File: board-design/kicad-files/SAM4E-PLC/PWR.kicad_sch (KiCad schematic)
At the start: 18 parts, among them Q1 BC817, U14 LM2576HVS-3.3

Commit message: [UPDATE]
Work in progress.

Signed-off-by: Nicolae-Andrei Vasile <vasilenicolaeandrei@gmail.com>
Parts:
- renumbered D35 to D36
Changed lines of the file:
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@@
         )
         (path "/93076d8a-73da-4f5d-b7f2-28678f1db77d/aee81a7b-cba1-4b89-a883-459d3f783e91"
-          (reference "C93") (unit 1)
+          (reference "C95") (unit 1)
         )
       )
@@
         )
         (path "/93076d8a-73da-4f5d-b7f2-28678f1db77d/aee81a7b-cba1-4b89-a883-459d3f783e91"
-          (reference "C90") (unit 1)
+          (reference "C92") (unit 1)
         )
       )
@@
         )
         (path "/93076d8a-73da-4f5d-b7f2-28678f1db77d/aee81a7b-cba1-4b89-a883-459d3f783e91"
-          (reference "C95") (unit 1)
+          (reference "C97") (unit 1)
         )
       )
@@
   (symbol (lib_id "power:GND") (at 234.95 133.35 0) (unit 1)
     (in_bom yes) (on_board yes) (dnp no) (fields_autoplaced)
-    (property "Reference" "#PWR085" (at 234.95 139.7 0)
+    (property "Reference" "#PWR086" (at 234.95 139.7 0)
       (effects (font (size 1.27 1.27)) hide)
     )
@@
       (project "SAM4E-PLC"
         (path "/93076d8a-73da-4f5d-b7f2-28678f1db77d/aee81a7b-cba1-4b89-a883-459d3f783e91"
-          (reference "#PWR085") (unit 1)
+          (reference "#PWR086") (unit 1)
         )
       )
@@
   (symbol (lib_id "power:+3V3") (at 245.11 93.98 0) (unit 1)
     (in_bom yes) (on_board yes) (dnp no) (fields_autoplaced)
-    (property "Reference" "#PWR086" (at 245.11 97.79 0)
+    (property "Reference" "#PWR087" (at 245.11 97.79 0)
       (effects (font (size 1.27 1.27)) hide)
     )
@@
       (project "SAM4E-PLC"
         (path "/93076d8a-73da-4f5d-b7f2-28678f1db77d/aee81a7b-cba1-4b89-a883-459d3f783e91"
-          (reference "#PWR086") (unit 1)
+          (reference "#PWR087") (unit 1)
         )
       )
@@
         )
         (path "/93076d8a-73da-4f5d-b7f2-28678f1db77d/aee81a7b-cba1-4b89-a883-459d3f783e91"
-          (reference "C91") (unit 1)
+          (reference "C93") (unit 1)
         )
       )
@@
         )
         (path "/93076d8a-73da-4f5d-b7f2-28678f1db77d/aee81a7b-cba1-4b89-a883-459d3f783e91"
-          (reference "D36") (unit 1)
+          (reference "D37") (unit 1)
         )
       )
@@
   (symbol (lib_id "power:+24V") (at 76.2 88.9 0) (unit 1)
     (in_bom yes) (on_board yes) (dnp no) (fields_autoplaced)
-    (property "Reference" "#PWR083" (at 76.2 92.71 0)
+    (property "Reference" "#PWR084" (at 76.2 92.71 0)
       (effects (font (size 1.27 1.27)) hide)
     )
@@
       (project "SAM4E-PLC"
         (path "/93076d8a-73da-4f5d-b7f2-28678f1db77d/aee81a7b-cba1-4b89-a883-459d3f783e91"
-          (reference "#PWR083") (unit 1)
+          (reference "#PWR084") (unit 1)
         )
       )
@@
   (symbol (lib_id "power:GND") (at 127 113.03 0) (unit 1)
     (in_bom yes) (on_board yes) (dnp no) (fields_autoplaced)
-    (property "Reference" "#PWR084" (at 127 119.38 0)
+    (property "Reference" "#PWR085" (at 127 119.38 0)
       (effects (font (size 1.27 1.27)) hide)
     )
@@
       (project "SAM4E-PLC"
         (path "/93076d8a-73da-4f5d-b7f2-28678f1db77d/aee81a7b-cba1-4b89-a883-459d3f783e91"
-          (reference "#PWR084") (unit 1)
+          (reference "#PWR085") (unit 1)
         )
       )
@@
         )
         (path "/93076d8a-73da-4f5d-b7f2-28678f1db77d/aee81a7b-cba1-4b89-a883-459d3f783e91"
-          (reference "C89") (unit 1)
+          (reference "C91") (unit 1)
         )
       )
@@
         )
         (path "/93076d8a-73da-4f5d-b7f2-28678f1db77d/aee81a7b-cba1-4b89-a883-459d3f783e91"
+          (reference "C96") (unit 1)
+        )
+      )
+    )
+  )
+  (symbol (lib_id "Device:L") (at 152.4 97.79 90) (unit 1)
+    (in_bom yes) (on_board yes) (dnp no)
+    (property "Reference" "L13" (at 152.4 95.25 90)
+      (effects (font (size 1.27 1.27)))
+    )
+    (property "Value" "150uH/12x12mm (SRR1210-151M)" (at 146.05 101.6 90)
+      (effects (font (size 1.27 1.27)))
+    )
+    (property "Footprint" "Inductor_SMD:L_12x12mm_H8mm" (at 152.4 97.79 0)
+      (effects (font (size 1.27 1.27)) hide)
+    )
+    (property "Datasheet" "https://ro.mouser.com/datasheet/2/54/srr1210-1391529.pdf" (at 152.4 97.79 0)
+      (effects (font (size 1.27 1.27)) hide)
+    )
+    (pin "1")
+    (pin "2")
+    (instances
+      (project "SAM4E-PLC"
+        (path "/93076d8a-73da-4f5d-b7f2-28678f1db77d/aee81a7b-cba1-4b89-a883-459d3f783e91"
+          (reference "L13") (unit 1)
+        )
+      )
+    )
+  )
+  (symbol (lib_id "Device:C_Polarized") (at 171.45 104.14 0) (unit 1)
+    (in_bom yes) (on_board yes) (dnp no)
+    (property "Reference" "C5" (at 172.72 109.22 90)
+      (effects (font (size 1.27 1.27)) (justify left))
+    )
+    (property "Value" "100uF/16V/20%/6.3x7.7mm" (at 172.72 101.6 90)
+      (effects (font (size 1.27 1.27)) (justify left))
+    )
+    (property "Footprint" "Capacitor_SMD:CP_Elec_6.3x7.7" (at 172.4152 107.95 0)
+      (effects (font (size 1.27 1.27)) hide)
+    )
+    (property "Datasheet" "~" (at 171.45 104.14 0)
+      (effects (font (size 1.27 1.27)) hide)
+    )
+    (pin "1")
+    (pin "2")
+    (instances
+      (project "SAM4E-PLC"
+        (path "/93076d8a-73da-4f5d-b7f2-28678f1db77d/32910dfe-b730-4651-8391-975b8cdac59d"
+          (reference "C5") (unit 1)
+        )
+        (path "/93076d8a-73da-4f5d-b7f2-28678f1db77d/62dc9d33-a289-4ad9-a327-b6290b31f4f3"
+          (reference "C12") (unit 1)
+        )
+        (path "/93076d8a-73da-4f5d-b7f2-28678f1db77d/aee81a7b-cba1-4b89-a883-459d3f783e91"
           (reference "C94") (unit 1)
         )
@@
     )
   )
-  (symbol (lib_id "Device:L") (at 152.4 97.79 90) (unit 1)
-    (in_bom yes) (on_board yes) (dnp no)
-    (property "Reference" "L13" (at 152.4 95.25 90)
-      (effects (font (size 1.27 1.27)))
-    )
-    (property "Value" "150uH/12x12mm (SRR1210-151M)" (at 146.05 101.6 90)
-      (effects (font (size 1.27 1.27)))
-    )
-    (property "Footprint" "Inductor_SMD:L_12x12mm_H8mm" (at 152.4 97.79 0)
-      (effects (font (size 1.27 1.27)) hide)
-    )
-    (property "Datasheet" "https://ro.mouser.com/datasheet/2/54/srr1210-1391529.pdf" (at 152.4 97.79 0)
-      (effects (font (size 1.27 1.27)) hide)
-    )
-    (pin "1")
-    (pin "2")
-    (instances
-      (project "SAM4E-PLC"
-        (path "/93076d8a-73da-4f5d-b7f2-28678f1db77d/aee81a7b-cba1-4b89-a883-459d3f783e91"
-          (reference "L13") (unit 1)
-        )
-      )
-    )
-  )
-  (symbol (lib_id "Device:C_Polarized") (at 171.45 104.14 0) (unit 1)
-    (in_bom yes) (on_board yes) (dnp no)
-    (property "Reference" "C5" (at 172.72 109.22 90)
-      (effects (font (size 1.27 1.27)) (justify left))
-    )
-    (property "Value" "100uF/16V/20%/6.3x7.7mm" (at 172.72 101.6 90)
-      (effects (font (size 1.27 1.27)) (justify left))
-    )
-    (property "Footprint" "Capacitor_SMD:CP_Elec_6.3x7.7" (at 172.4152 107.95 0)
-      (effects (font (size 1.27 1.27)) hide)
-    )
-    (property "Datasheet" "~" (at 171.45 104.14 0)
-      (effects (font (size 1.27 1.27)) hide)
-    )
-    (pin "1")
-    (pin "2")
-    (instances
-      (project "SAM4E-PLC"
-        (path "/93076d8a-73da-4f5d-b7f2-28678f1db77d/32910dfe-b730-4651-8391-975b8cdac59d"
-          (reference "C5") (unit 1)
-        )
-        (path "/93076d8a-73da-4f5d-b7f2-28678f1db77d/62dc9d33-a289-4ad9-a327-b6290b31f4f3"
-          (reference "C12") (unit 1)
-        )
-        (path "/93076d8a-73da-4f5d-b7f2-28678f1db77d/aee81a7b-cba1-4b89-a883-459d3f783e91"
-          (reference "C92") (unit 1)
-        )
-      )
-    )
-  )
   (symbol (lib_id "Device:LED") (at 234.95 114.3 90) (unit 1)
     (in_bom yes) (on_board yes) (dnp no)
@@
         )
         (path "/93076d8a-73da-4f5d-b7f2-28678f1db77d/aee81a7b-cba1-4b89-a883-459d3f783e91"
-          (reference "D37") (unit 1)
+          (reference "D38") (unit 1)
         )
       )
@@
   (symbol (lib_id "Device:D_Schottky") (at 63.5 92.71 180) (unit 1)
     (in_bom yes) (on_board yes) (dnp no)
-    (property "Reference" "D35" (at 63.5 87.63 0)
+    (property "Reference" "D36" (at 63.5 87.63 0)
       (effects (font (size 1.27 1.27)))
     )
@@
       (project "SAM4E-PLC"
         (path "/93076d8a-73da-4f5d-b7f2-28678f1db77d/aee81a7b-cba1-4b89-a883-459d3f783e91"
-          (reference "D35") (unit 1)
-        )
-      )
+          (reference "D36") (unit 1)
+        )
+      )

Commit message: [UPDATE]
Work in progress.

Signed-off-by: Nicolae-Andrei Vasile <vasilenicolaeandrei@gmail.com>
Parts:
- renumbered D36 to D34, L13 to L10, U14 to U11
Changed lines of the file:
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@@
           (reference "C5") (unit 1)
         )
-        (path "/93076d8a-73da-4f5d-b7f2-28678f1db77d/62dc9d33-a289-4ad9-a327-b6290b31f4f3"
-          (reference "C12") (unit 1)
-        )
-        (path "/93076d8a-73da-4f5d-b7f2-28678f1db77d/aee81a7b-cba1-4b89-a883-459d3f783e91"
-          (reference "C95") (unit 1)
+        (path "/93076d8a-73da-4f5d-b7f2-28678f1db77d/aee81a7b-cba1-4b89-a883-459d3f783e91"
+          (reference "C71") (unit 1)
         )
       )
@@
           (reference "C5") (unit 1)
         )
-        (path "/93076d8a-73da-4f5d-b7f2-28678f1db77d/62dc9d33-a289-4ad9-a327-b6290b31f4f3"
-          (reference "C12") (unit 1)
-        )
-        (path "/93076d8a-73da-4f5d-b7f2-28678f1db77d/aee81a7b-cba1-4b89-a883-459d3f783e91"
-          (reference "C92") (unit 1)
+        (path "/93076d8a-73da-4f5d-b7f2-28678f1db77d/aee81a7b-cba1-4b89-a883-459d3f783e91"
+          (reference "C68") (unit 1)
         )
       )
@@
         )
         (path "/93076d8a-73da-4f5d-b7f2-28678f1db77d/aee81a7b-cba1-4b89-a883-459d3f783e91"
-          (reference "C97") (unit 1)
+          (reference "C73") (unit 1)
         )
       )
@@
   (symbol (lib_id "power:GND") (at 234.95 133.35 0) (unit 1)
     (in_bom yes) (on_board yes) (dnp no) (fields_autoplaced)
-    (property "Reference" "#PWR086" (at 234.95 139.7 0)
+    (property "Reference" "#PWR070" (at 234.95 139.7 0)
       (effects (font (size 1.27 1.27)) hide)
     )
@@
       (project "SAM4E-PLC"
         (path "/93076d8a-73da-4f5d-b7f2-28678f1db77d/aee81a7b-cba1-4b89-a883-459d3f783e91"
-          (reference "#PWR086") (unit 1)
+          (reference "#PWR070") (unit 1)
         )
       )
@@
   (symbol (lib_id "power:+3V3") (at 245.11 93.98 0) (unit 1)
     (in_bom yes) (on_board yes) (dnp no) (fields_autoplaced)
-    (property "Reference" "#PWR087" (at 245.11 97.79 0)
+    (property "Reference" "#PWR071" (at 245.11 97.79 0)
       (effects (font (size 1.27 1.27)) hide)
     )
@@
       (project "SAM4E-PLC"
         (path "/93076d8a-73da-4f5d-b7f2-28678f1db77d/aee81a7b-cba1-4b89-a883-459d3f783e91"
-          (reference "#PWR087") (unit 1)
+          (reference "#PWR071") (unit 1)
         )
       )
@@
           (reference "C5") (unit 1)
         )
-        (path "/93076d8a-73da-4f5d-b7f2-28678f1db77d/62dc9d33-a289-4ad9-a327-b6290b31f4f3"
-          (reference "C12") (unit 1)
-        )
-        (path "/93076d8a-73da-4f5d-b7f2-28678f1db77d/aee81a7b-cba1-4b89-a883-459d3f783e91"
-          (reference "C93") (unit 1)
+        (path "/93076d8a-73da-4f5d-b7f2-28678f1db77d/aee81a7b-cba1-4b89-a883-459d3f783e91"
+          (reference "C69") (unit 1)
         )
       )
@@
     (instances
       (project "SAM4E-PLC"
-        (path "/93076d8a-73da-4f5d-b7f2-28678f1db77d/62dc9d33-a289-4ad9-a327-b6290b31f4f3"
-          (reference "D3") (unit 1)
-        )
-        (path "/93076d8a-73da-4f5d-b7f2-28678f1db77d/aee81a7b-cba1-4b89-a883-459d3f783e91"
-          (reference "D37") (unit 1)
+        (path "/93076d8a-73da-4f5d-b7f2-28678f1db77d/aee81a7b-cba1-4b89-a883-459d3f783e91"
+          (reference "D35") (unit 1)
         )
       )
@@
   (symbol (lib_id "power:+24V") (at 76.2 88.9 0) (unit 1)
     (in_bom yes) (on_board yes) (dnp no) (fields_autoplaced)
-    (property "Reference" "#PWR084" (at 76.2 92.71 0)
+    (property "Reference" "#PWR068" (at 76.2 92.71 0)
       (effects (font (size 1.27 1.27)) hide)
     )
@@
       (project "SAM4E-PLC"
         (path "/93076d8a-73da-4f5d-b7f2-28678f1db77d/aee81a7b-cba1-4b89-a883-459d3f783e91"
-          (reference "#PWR084") (unit 1)
+          (reference "#PWR068") (unit 1)
         )
       )
@@
   (symbol (lib_id "power:GND") (at 127 113.03 0) (unit 1)
     (in_bom yes) (on_board yes) (dnp no) (fields_autoplaced)
-    (property "Reference" "#PWR085" (at 127 119.38 0)
+    (property "Reference" "#PWR069" (at 127 119.38 0)
       (effects (font (size 1.27 1.27)) hide)
     )
@@
       (project "SAM4E-PLC"
         (path "/93076d8a-73da-4f5d-b7f2-28678f1db77d/aee81a7b-cba1-4b89-a883-459d3f783e91"
-          (reference "#PWR085") (unit 1)
+          (reference "#PWR069") (unit 1)
         )
       )
@@
   (symbol (lib_id "Regulator_Switching:LM2576HVS-3.3") (at 127 95.25 0) (unit 1)
     (in_bom yes) (on_board yes) (dnp no) (fields_autoplaced)
-    (property "Reference" "U14" (at 127 85.09 0)
+    (property "Reference" "U11" (at 127 85.09 0)
       (effects (font (size 1.27 1.27)))
     )
@@
       (project "SAM4E-PLC"
         (path "/93076d8a-73da-4f5d-b7f2-28678f1db77d/aee81a7b-cba1-4b89-a883-459d3f783e91"
-          (reference "U14") (unit 1)
+          (reference "U11") (unit 1)
         )
       )
@@
     (instances
       (project "SAM4E-PLC"
-        (path "/93076d8a-73da-4f5d-b7f2-28678f1db77d/62dc9d33-a289-4ad9-a327-b6290b31f4f3"
-          (reference "Q1") (unit 1)
-        )
-        (path "/93076d8a-73da-4f5d-b7f2-28678f1db77d/aee81a7b-cba1-4b89-a883-459d3f783e91"
-          (reference "Q13") (unit 1)
+        (path "/93076d8a-73da-4f5d-b7f2-28678f1db77d/aee81a7b-cba1-4b89-a883-459d3f783e91"
+          (reference "Q11") (unit 1)
         )
       )
@@
           (reference "C5") (unit 1)
         )
-        (path "/93076d8a-73da-4f5d-b7f2-28678f1db77d/62dc9d33-a289-4ad9-a327-b6290b31f4f3"
-          (reference "C12") (unit 1)
-        )
-        (path "/93076d8a-73da-4f5d-b7f2-28678f1db77d/aee81a7b-cba1-4b89-a883-459d3f783e91"
-          (reference "C91") (unit 1)
+        (path "/93076d8a-73da-4f5d-b7f2-28678f1db77d/aee81a7b-cba1-4b89-a883-459d3f783e91"
+          (reference "C67") (unit 1)
         )
       )
@@
           (reference "R9") (unit 1)
         )
-        (path "/93076d8a-73da-4f5d-b7f2-28678f1db77d/62dc9d33-a289-4ad9-a327-b6290b31f4f3"
-          (reference "R?") (unit 1)
-        )
         (path "/93076d8a-73da-4f5d-b7f2-28678f1db77d/f76e13f7-6a24-4ea6-98c5-a4d0bd3b3ced"
           (reference "R88") (unit 1)
         )
         (path "/93076d8a-73da-4f5d-b7f2-28678f1db77d/aee81a7b-cba1-4b89-a883-459d3f783e91"
-          (reference "R112") (unit 1)
+          (reference "R87") (unit 1)
         )
       )
@@
           (reference "R9") (unit 1)
         )
-        (path "/93076d8a-73da-4f5d-b7f2-28678f1db77d/62dc9d33-a289-4ad9-a327-b6290b31f4f3"
-          (reference "R?") (unit 1)
-        )
         (path "/93076d8a-73da-4f5d-b7f2-28678f1db77d/f76e13f7-6a24-4ea6-98c5-a4d0bd3b3ced"
           (reference "R88") (unit 1)
         )
         (path "/93076d8a-73da-4f5d-b7f2-28678f1db77d/aee81a7b-cba1-4b89-a883-459d3f783e91"
-          (reference "R113") (unit 1)
+          (reference "R88") (unit 1)
         )
       )
@@
       )
       (project "SAM4E-PLC"
-        (path "/93076d8a-73da-4f5d-b7f2-28678f1db77d/62dc9d33-a289-4ad9-a327-b6290b31f4f3"
-          (reference "R?") (unit 1)
-        )
         (path "/93076d8a-73da-4f5d-b7f2-28678f1db77d/f76e13f7-6a24-4ea6-98c5-a4d0bd3b3ced"
           (reference "R53") (unit 1)
         )
         (path "/93076d8a-73da-4f5d-b7f2-28678f1db77d/aee81a7b-cba1-4b89-a883-459d3f783e91"
-          (reference "R114") (unit 1)
+          (reference "R89") (unit 1)
         )
       )
@@
         )
         (path "/93076d8a-73da-4f5d-b7f2-28678f1db77d/aee81a7b-cba1-4b89-a883-459d3f783e91"
-          (reference "C96") (unit 1)
+          (reference "C72") (unit 1)
         )
       )
@@
   (symbol (lib_id "Device:L") (at 152.4 97.79 90) (unit 1)
     (in_bom yes) (on_board yes) (dnp no)
-    (property "Reference" "L13" (at 152.4 95.25 90)
+    (property "Reference" "L10" (at 152.4 95.25 90)
       (effects (font (size 1.27 1.27)))
     )
@@
       (project "SAM4E-PLC"
         (path "/93076d8a-73da-4f5d-b7f2-28678f1db77d/aee81a7b-cba1-4b89-a883-459d3f783e91"
-          (reference "L13") (unit 1)
+          (reference "L10") (unit 1)
         )
       )
@@
           (reference "C5") (unit 1)
         )
-        (path "/93076d8a-73da-4f5d-b7f2-28678f1db77d/62dc9d33-a289-4ad9-a327-b6290b31f4f3"
-          (reference "C12") (unit 1)
-        )
-        (path "/93076d8a-73da-4f5d-b7f2-28678f1db77d/aee81a7b-cba1-4b89-a883-459d3f783e91"
-          (reference "C94") (unit 1)
+        (path "/93076d8a-73da-4f5d-b7f2-28678f1db77d/aee81a7b-cba1-4b89-a883-459d3f783e91"
+          (reference "C70") (unit 1)
         )
       )
@@
         )
         (path "/93076d8a-73da-4f5d-b7f2-28678f1db77d/aee81a7b-cba1-4b89-a883-459d3f783e91"
-          (reference "D38") (unit 1)
+          (reference "D36") (unit 1)
         )
       )
@@
         )
         (path "/93076d8a-73da-4f5d-b7f2-28678f1db77d/aee81a7b-cba1-4b89-a883-459d3f783e91"
-          (reference "R111") (unit 1)
+          (reference "R86") (unit 1)
         )
       )
@@
         )
         (path "/93076d8a-73da-4f5d-b7f2-28678f1db77d/aee81a7b-cba1-4b89-a883-459d3f783e91"
-          (reference "#FLG017") (unit 1)
+          (reference "#FLG013") (unit 1)
         )
       )
@@
   (symbol (lib_id "Device:D_Schottky") (at 63.5 92.71 180) (unit 1)
     (in_bom yes) (on_board yes) (dnp no)
-    (property "Reference" "D36" (at 63.5 87.63 0)
+    (property "Reference" "D34" (at 63.5 87.63 0)
       (effects (font (size 1.27 1.27)))
     )
@@
       (project "SAM4E-PLC"
         (path "/93076d8a-73da-4f5d-b7f2-28678f1db77d/aee81a7b-cba1-4b89-a883-459d3f783e91"
-          (reference "D36") (unit 1)
-        )
-      )
+          (reference "D34") (unit 1)
+        )
+      )

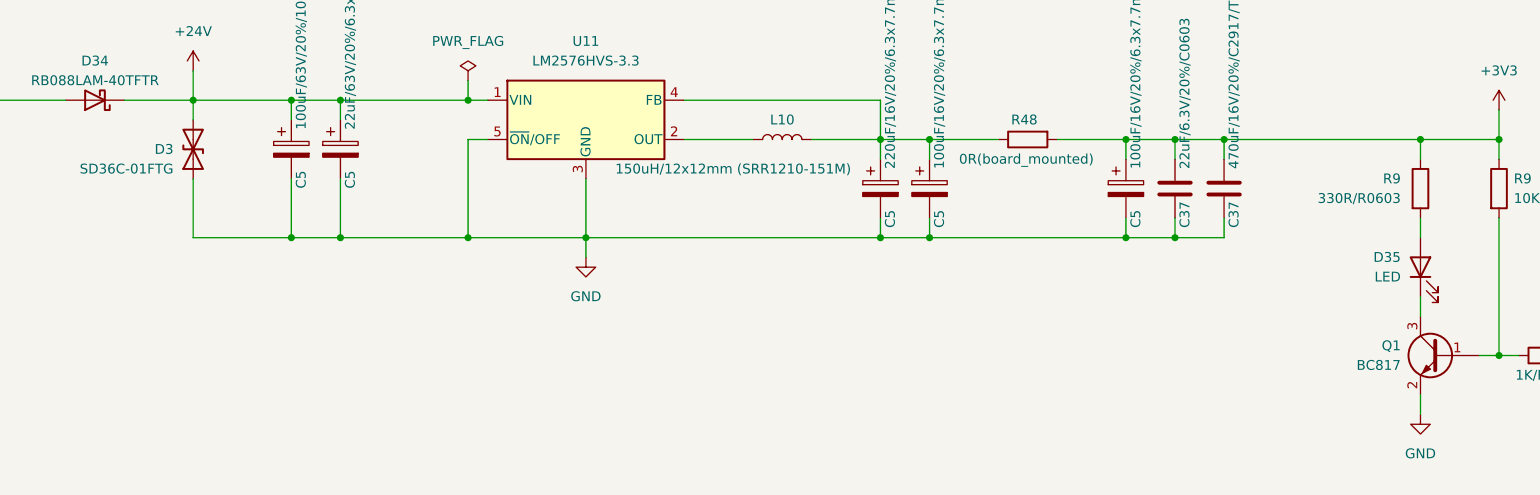
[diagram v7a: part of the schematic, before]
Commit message: [UPDATE]
Completed SAM4E-PLC board design.

Signed-off-by: Nicolae-Andrei Vasile <vasilenicolaeandrei@gmail.com>
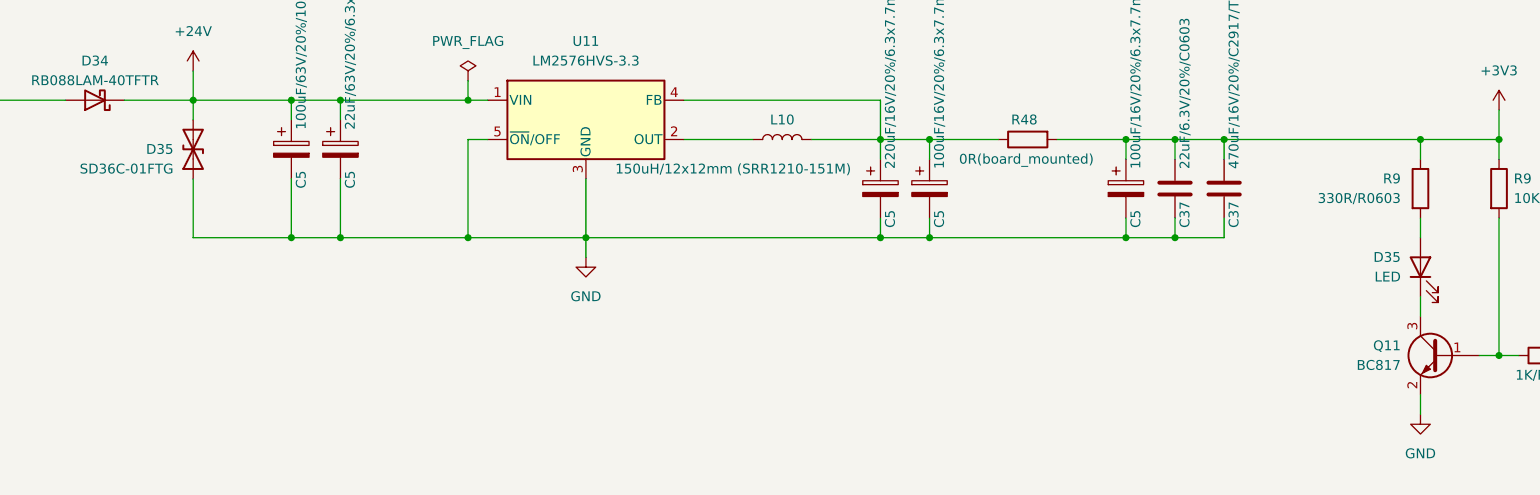
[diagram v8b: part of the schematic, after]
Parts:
- renumbered D3 to D35, Q1 to Q11
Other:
- title: Power Supply -> SAM4E
